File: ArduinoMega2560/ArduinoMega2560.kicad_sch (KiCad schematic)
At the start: 25 parts, among them J1 Conn_02x08, J2 Conn_02x08, Q2 Crystal_16MHz, SW1 Push_Button, U1 ATmega2560-16A, Y1 TSX-3225_16.0000MF18X-AC0

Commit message: Update
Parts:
- added J5: Conn_02x08, PCM_4ms_Connector:Pins_2x08_2.54mm_TH, symbol PCM_4ms_Connector:Conn_02x08
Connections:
- net ADC0: now also ADC2.8; no longer ADC1.1
- net ADC1: now also ADC2.7; no longer ADC1.2
- net ADC10: now also ADC1.6; no longer ADC2.3
- net ADC11: now also ADC1.5; no longer ADC2.4
- net ADC12: now also ADC1.4; no longer ADC2.5
- net ADC13: now also ADC1.3; no longer ADC2.6
- net ADC14: now also ADC1.2; no longer ADC2.7
- net ADC15: now also ADC1.1; no longer ADC2.8
- net ADC2: now also ADC2.6; no longer ADC1.3
- net ADC3: now also ADC2.5; no longer ADC1.4
- net ADC4: now also ADC2.4; no longer ADC1.5
- net ADC5: now also ADC2.3; no longer ADC1.6
- net ADC6: now also ADC2.2; no longer ADC1.7
- net ADC7: now also ADC2.1; no longer ADC1.8
- net ADC8: now also ADC1.8; no longer ADC2.1
- net ADC9: now also ADC1.7; no longer ADC2.2
- net PH2: now reaches U1.14 (PH2)
- net PH2: now also J5.13 (-12)
- net PH7: now reaches U1.27 (PH7)
- net PH7: now also J5.15 (-12V)
- net PG3: now reaches U1.28 (PG3)
- net PG3: now also J5.14 (-12V)
- net PG4: now reaches U1.29 (PG4)
- net PG4: now also J5.16 (P16)
- net PE2: now reaches U1.4 (PE2)
- net PE2: now also J5.8 (+12V)
- net PD4: now reaches U1.47 (PD4)
- net PD4: now also J5.2 (P2)
- net PD5: now reaches U1.48 (PD5)
- net PD5: now also J5.4 (P4)
- net PD6: now reaches U1.49 (PD6)
- net PD6: now also J5.6 (P6)
- net PJ2: now reaches U1.65 (PJ2)
- net PJ3: now reaches U1.66 (PJ3)
- net PJ4: now reaches U1.67 (PJ4)
- net PJ5: now reaches U1.68 (PJ5)
- net PJ6: now reaches U1.69 (PJ6)
- net PJ7: now reaches U1.79 (PJ7)
- net PE6: now reaches U1.8 (PE6)
- net PE6: now also J5.10 (GND)
- net PE7: now reaches U1.9 (PE7)
- net PE7: now also J5.12 (GND)
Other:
- moved on the sheet: ADC1, ADC2

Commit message: Update
Using Rev3
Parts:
- removed C14, C15: 22pF_0603_16V, PCM_4ms_Capacitor:C_0603, symbol PCM_4ms_Capacitor:100nF_0603_16V
- removed PWR1: PINHD_1x6_Male, Connector_PinHeader_2.54mm:PinHeader_1x06_P2.54mm_Vertical, symbol PCM_SL_Pin_Headers:PINHD_1x6_Male
- removed Q2: Crystal_16MHz, Crystal:Crystal_HC49-4H_Vertical, symbol PCM_SL_Devices:Crystal_16MHz
- removed R3: 27R_0603, PCM_Resistor_SMD_AKL:R_0603_1608Metric, symbol PCM_Resistor_AKL:R_0603
- removed Y1: TSX-3225_16.0000MF18X-AC0, EPSON_TSX-3225-16MF18X-AC0:XTAL_TSX-3225_16.0000MF18X-AC0, symbol EPSON-TSX-3225-16MF18X-AC0:TSX-3225_16.0000MF18X-AC0
- added C16: 100nF_0603_16V, PCM_4ms_Capacitor:C_0603, symbol PCM_4ms_Capacitor:100nF_0603_16V
- added D3: CD1206-S01575, Diode_CD1206-S01575_Bourns:DIODE_CD1206-S01575_BRN, symbol Diode_CD1206-S01575_Bourns:CD1206-S01575
- added J3, J4: PINHD_1x2_Male, Connector_PinHeader_2.54mm:PinHeader_1x02_P2.54mm_Vertical, symbol PCM_SL_Pin_Headers:PINHD_1x2_Male
- added L2: MH2029-300Y, FerriteBead_MH2029-300Y_Bourns:IND_BOURNS_MH2029, symbol FerriteBead_MH2029-300Y_Bourns:MH2029-300Y
- added PWR1: PINHD_1x8_Female, Connector_PinSocket_2.54mm:PinSocket_1x08_P2.54mm_Vertical, symbol PCM_SL_Pin_Headers:PINHD_1x8_Female
- added Y1: CSTCE16M0V53-R0, Resonators_CSTCE16M0V53-R0_Murata:OSC_CSTCE16M0V53-R0, symbol Resonators_CSTCE16M0V53-R0_Murata:CSTCE16M0V53-R0
- renumbered ICSP2 to ICSP1, RN11 to RN51
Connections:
- net +3V3: now also PWR1.4
- net +5V: now also D3.1, J3.1, J3.2, L2.2, PWR1.2, PWR1.5; no longer U1.100 (AVCC)
- net GND: now also C16.2, J4.1, J4.2, PWR1.6, PWR1.7, Y1.2
- net RESET1: now also D3.2, PWR1.3
- net VIN: now also PWR1.8
- net at R1.1, U1.33 (XTAL2): now also Y1.3
- net at R1.2: now also U1.34 (XTAL1), Y1.1
- new net AVCC: C16.1, L2.1, U1.100 (AVCC)
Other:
- moved on the sheet: C1, J2, RN51, SW1

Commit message: Update
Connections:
- net RX2 is gone; now on net RXD2: U1.12 (PH0)
- net RX3 is gone; now on net RXD3: U1.63 (PJ0)
- net TX2 is gone; now on net TXD2: U1.13 (PH1)
- net TX3 is gone; now on net TXD3: U1.64 (PJ1)
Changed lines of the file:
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@@
 		)
 	)
-	(hierarchical_label "RX2"
+	(hierarchical_label "RXD2"
 		(shape input)
 		(at 193.04 146.05 180)
@@
 		)
 	)
-	(hierarchical_label "RX3"
+	(hierarchical_label "RXD3"
 		(shape input)
 		(at 193.04 123.19 180)
@@
 		)
 	)
-	(hierarchical_label "TX2"
+	(hierarchical_label "TXD2"
 		(shape input)
 		(at 193.04 148.59 180)
@@
 		)
 	)
-	(hierarchical_label "TX3"
+	(hierarchical_label "TXD3"
 		(shape input)
 		(at 193.04 125.73 180)

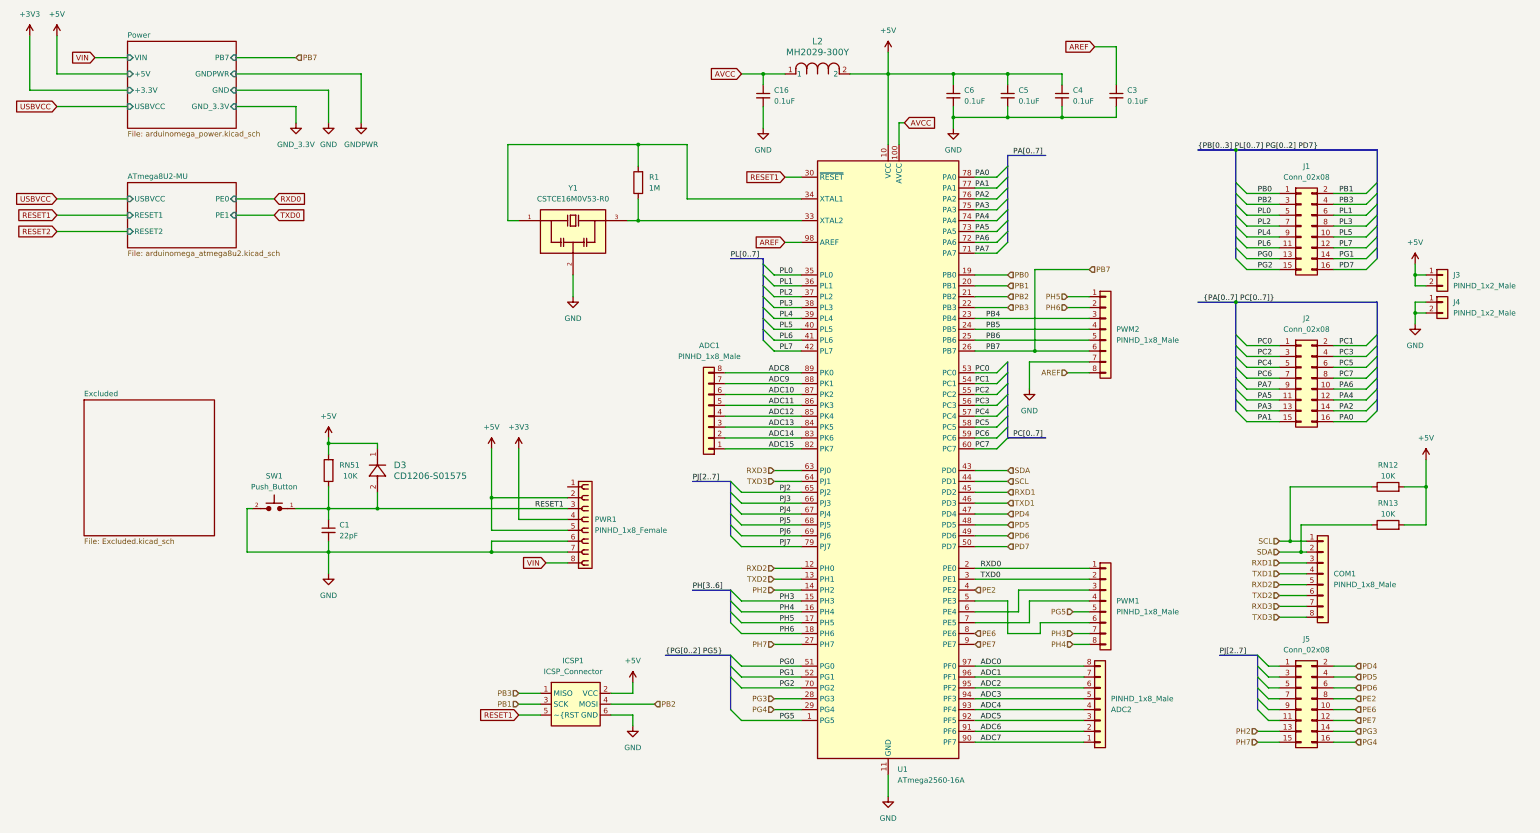
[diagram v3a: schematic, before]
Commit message: Update footprint and silkscree
next, fixing the trace on the pinheader
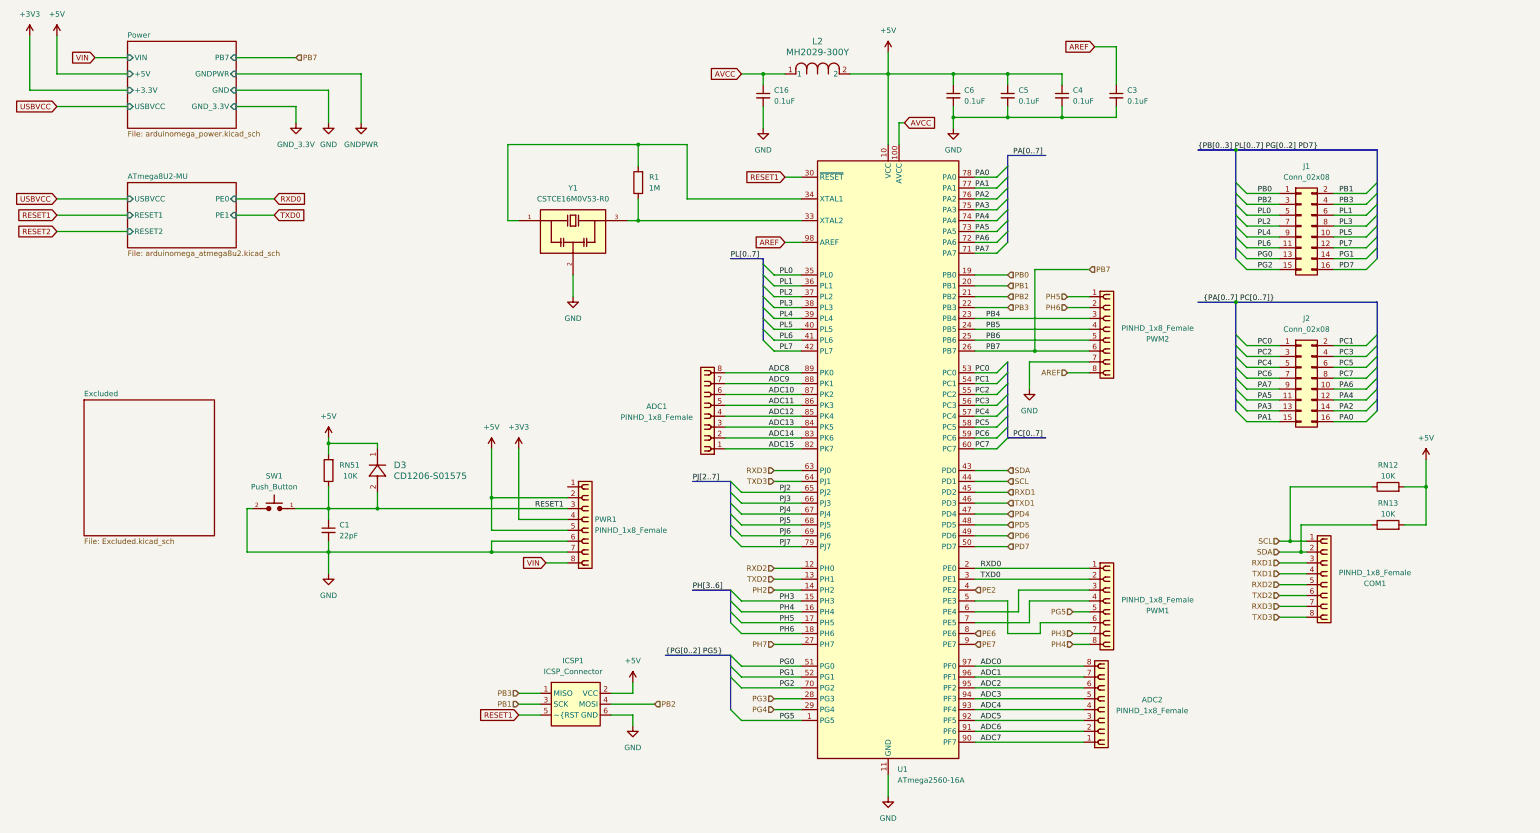
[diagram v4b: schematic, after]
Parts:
- removed ADC1, ADC2, COM1, PWM1, PWM2: PINHD_1x8_Male, Connector_PinHeader_2.54mm:PinHeader_1x08_P2.54mm_Vertical, symbol PCM_SL_Pin_Headers:PINHD_1x8_Male
- removed J3, J4: PINHD_1x2_Male, Connector_PinHeader_2.54mm:PinHeader_1x02_P2.54mm_Vertical, symbol PCM_SL_Pin_Headers:PINHD_1x2_Male
- removed J5: Conn_02x08, PCM_4ms_Connector:Pins_2x08_2.54mm_TH, symbol PCM_4ms_Connector:Conn_02x08
- added ADC1, ADC2, COM1, PWM1, PWM2: PINHD_1x8_Female, Connector_PinSocket_2.54mm:PinSocket_1x08_P2.54mm_Vertical, symbol PCM_SL_Pin_Headers:PINHD_1x8_Female
- J1, J2: footprint PCM_4ms_Connector:Pins_2x08_2.54mm_TH -> Connector_PinSocket_2.54mm:PinSocket_2x08_P2.54mm_Vertical
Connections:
- net ADC0: now also ADC2.8
- net ADC1: now also ADC2.7
- net ADC10: now also ADC1.6
- net ADC11: now also ADC1.5
- net ADC12: now also ADC1.4
- net ADC13: now also ADC1.3
- net ADC14: now also ADC1.2
- net ADC15: now also ADC1.1
- net ADC2: now also ADC2.6
- net ADC3: now also ADC2.5
- net ADC4: now also ADC2.4
- net ADC5: now also ADC2.3
- net ADC6: now also ADC2.2
- net ADC7: now also ADC2.1
- net ADC8: now also ADC1.8
- net ADC9: now also ADC1.7
- net AREF: now also PWM2.8
- net GND: now also PWM2.7
- net PB4: now also PWM2.3
- net PB5: now also PWM2.4
- net PB6: now also PWM2.5
- net PB7: now also PWM2.6
- net PG5: now also PWM1.5
- net PH3: now also PWM1.7
- net PH4: now also PWM1.8
- net PH5: now also PWM2.1
- net PH6: now also PWM2.2
- net RXD0: now also PWM1.1
- net RXD1: now also COM1.3
- net RXD2: now also COM1.5
- net RXD3: now also COM1.7
- net SCL: now also COM1.1
- net SDA: now also COM1.2
- net TXD0: now also PWM1.2
- net TXD1: now also COM1.4
- net TXD2: now also COM1.6
- net TXD3: now also COM1.8
- net at U1.5 (PE3): now also PWM1.6
- net at U1.6 (PE4): now also PWM1.3
- net at U1.7 (PE5): now also PWM1.4

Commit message: Update Eth
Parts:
- added J3, J4: PINHD_1x2_Female, Connector_PinSocket_2.54mm:PinSocket_1x02_P2.54mm_Vertical, symbol PCM_SL_Pin_Headers:PINHD_1x2_Female
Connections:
- net +5V: now also J3.1, J3.2
- net GND: now also J4.1, J4.2
